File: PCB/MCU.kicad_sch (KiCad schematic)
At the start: 42 parts, among them J1 SWD, J10 GPIO2, J2 TC2030-NL, J3 VIK Keyboard Expansion, J4 OLED Breakout, J7 GND, J8 3V3, J9 GPIO3, SW1 PTS645, SW2 PTS645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

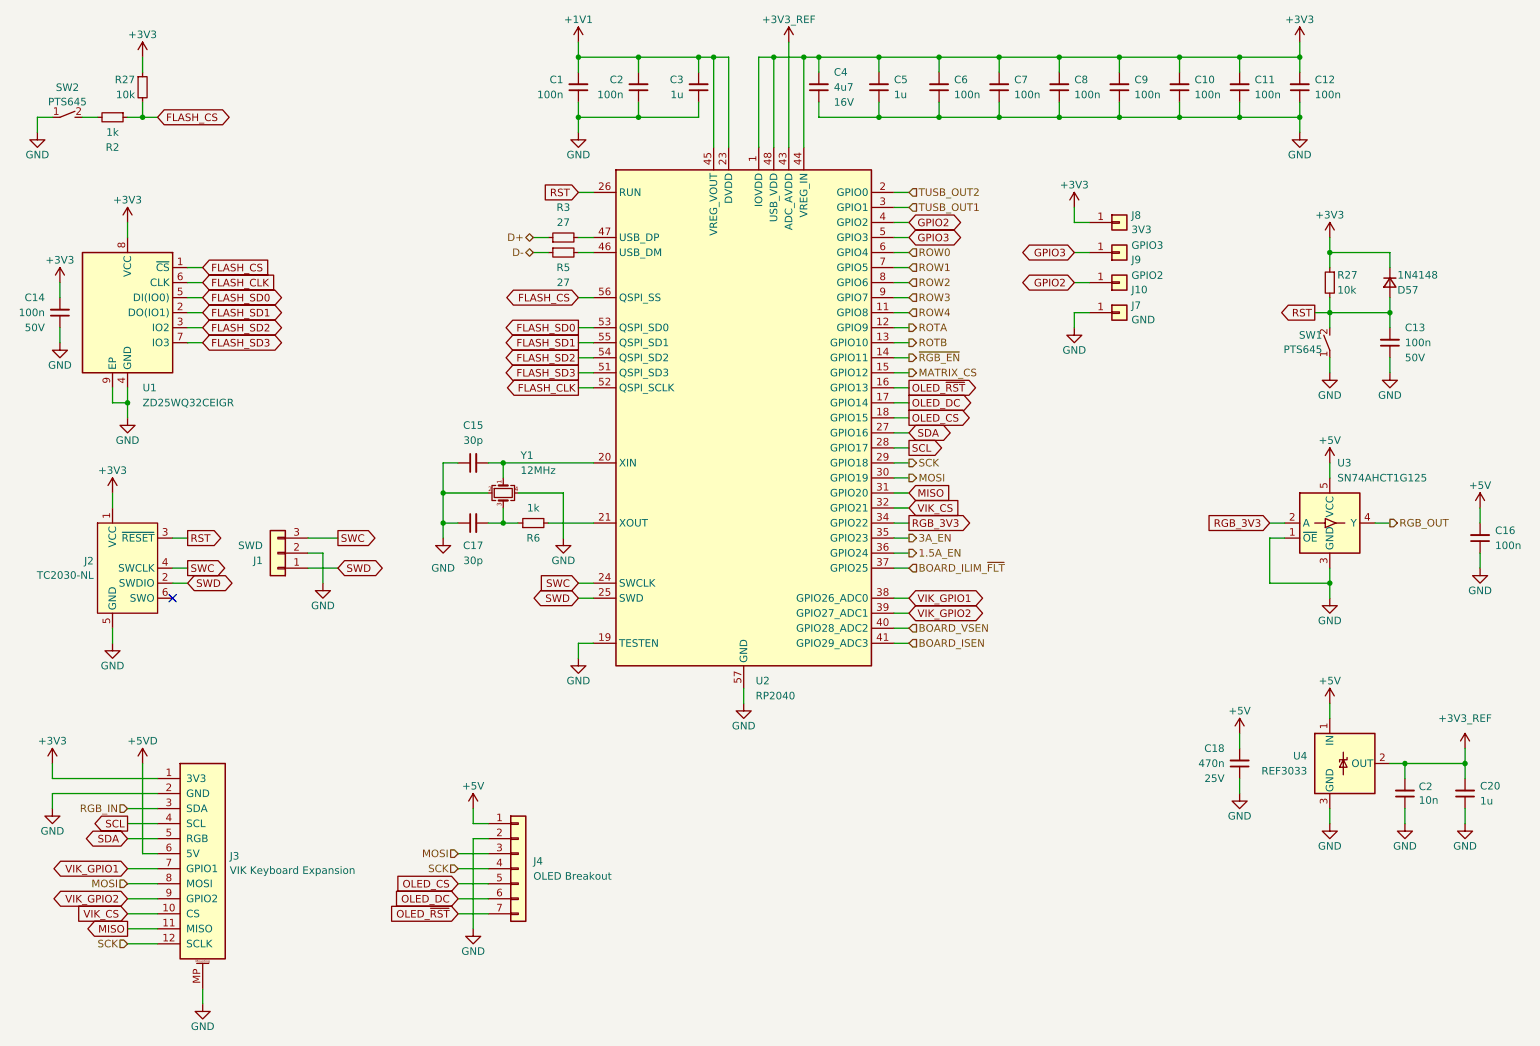
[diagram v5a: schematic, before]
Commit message: 16/08/2023 update
Updated to V3.1. Fixed VIK wiring (RGB and SDA were swapped). Added another BAV70 for the bottom button in the thumb cluster. Added DNP attribute to R15. Added jumper for VIK 5V rail.
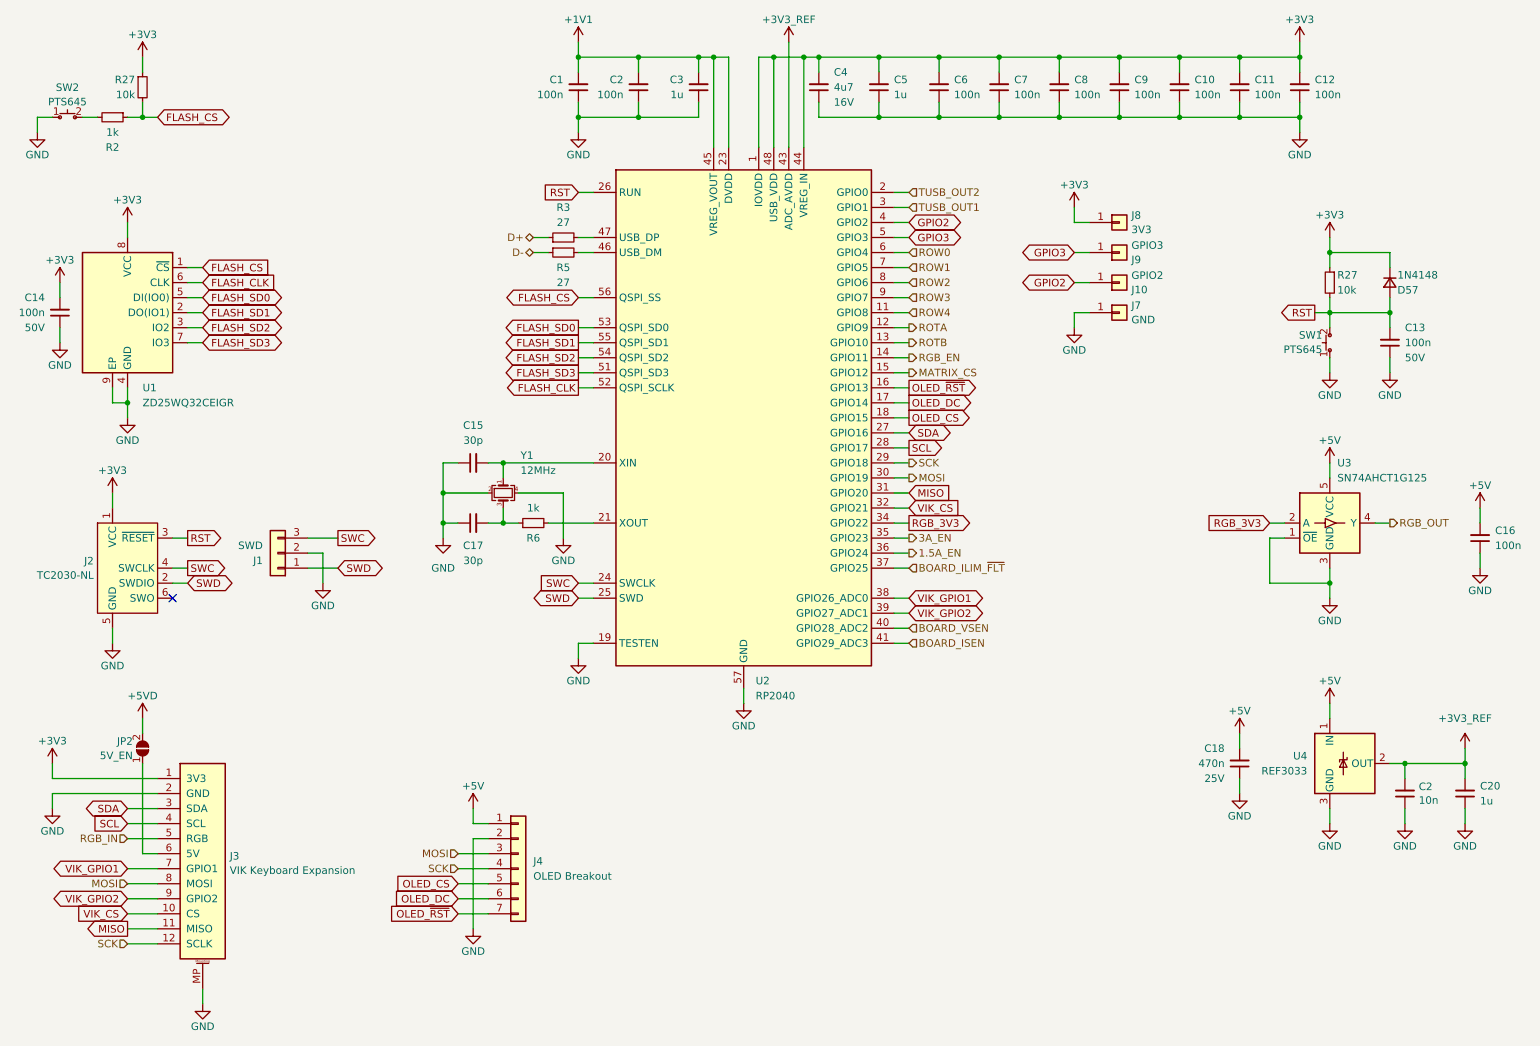
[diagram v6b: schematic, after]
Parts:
- added JP2: 5V_EN, Jumper:SolderJumper-2_P1.3mm_Open_Pad1.0x1.5mm, symbol Honeydew:SolderJumper_2_Open
- SW1, SW2: symbol Cantaloupe:SW_SPST_Small -> Honeydew:SW_SPST_Small
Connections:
- net +5VD: now also JP2.2 (B); no longer J3.6 (5V)
- net RGB_IN: now also J3.5 (RGB); no longer J3.3 (SDA)
- net SDA: now also J3.3 (SDA); no longer J3.5 (RGB)
- net ~{RGB_EN} renamed RGB_EN
- new net: J3.6 (5V), JP2.1 (A)
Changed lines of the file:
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@@
   (title_block
     (title "Honeydew unified split ergonomic keyboard")
-    (date "2023-08-06")
-    (rev "V3.0")
+    (date "2023-08-16")
+    (rev "V3.1")
     (company "Created by Ariamelon (https://github.com/Ariamelon/Honeydew/)")
     (comment 1 "All capacitors 50V unless otherwise specified.")
-    (comment 2 "Licensed under CC BY 4.0.")
+    (comment 2 "Follows the VIK standard by Sadek Baroudi (https://github.com/sadekbaroudi/VIK)")
+    (comment 3 "Licensed under CC BY 4.0.")
   )
   (junction (at 180.34 35.56) (diameter 0) (color 0 0 0 0)
@@
     (stroke (width 0) (type default))
   )
+  (wire (pts (xy 35.56 144.78) (xy 35.56 160.02))
+    (stroke (width 0) (type default))
+  )
   (wire (pts (xy 149.86 25.4) (xy 160.02 25.4))
     (stroke (width 0) (type default))
@@
     (stroke (width 0) (type default))
   )
-  (wire (pts (xy 35.56 144.78) (xy 35.56 160.02))
+  (wire (pts (xy 35.56 137.16) (xy 35.56 139.7))
     (stroke (width 0) (type default))
   )
@@
     )
   )
-  (global_label "SDA" (shape bidirectional) (at 33.02 157.48 180) (fields_autoplaced)
+  (global_label "SDA" (shape bidirectional) (at 33.02 152.4 180) (fields_autoplaced)
     (effects (font (size 1.27 1.27)) (justify right))
-    (property "Intersheetrefs" "${INTERSHEET_REFS}" (at 26.1684 157.48 0)
+    (property "Intersheetrefs" "${INTERSHEET_REFS}" (at 26.1684 152.4 0)
       (effects (font (size 1.27 1.27)) (justify right) hide)
     )
@@
     )
   )
-  (global_label "SCL" (shape output) (at 33.02 154.94 180) (fields_autoplaced)
+  (global_label "SCL" (shape input) (at 33.02 154.94 180) (fields_autoplaced)
     (effects (font (size 1.27 1.27)) (justify right))
     (property "Intersheetrefs" "${INTERSHEET_REFS}" (at 27.1814 154.94 0)
@@
     (effects (font (size 1.27 1.27)) (justify right))
   )
-  (hierarchical_label "RGB_IN" (shape input) (at 33.02 152.4 180) (fields_autoplaced)
+  (hierarchical_label "RGB_IN" (shape input) (at 33.02 157.48 180) (fields_autoplaced)
     (effects (font (size 1.27 1.27)) (justify right))
   )
@@
     (effects (font (size 1.27 1.27)) (justify left))
   )
-  (hierarchical_label "~{RGB_EN}" (shape output) (at 165.1 76.2 0) (fields_autoplaced)
+  (hierarchical_label "RGB_EN" (shape output) (at 165.1 76.2 0) (fields_autoplaced)
     (effects (font (size 1.27 1.27)) (justify left))
   )
@@
     )
   )
-  (symbol (lib_id "Cantaloupe:SW_SPST_Small") (at 236.22 73.66 90) (unit 1)
+  (symbol (lib_id "Honeydew:SW_SPST_Small") (at 236.22 73.66 90) (unit 1)
     (in_bom yes) (on_board yes) (dnp no)
     (property "Reference" "SW1" (at 234.95 72.39 90)
@@
       (effects (font (size 1.524 1.524)) hide)
     )
-    (property "Datasheet" "" (at 231.14 73.66 0)
+    (property "Datasheet" "~" (at 231.14 73.66 0)
       (effects (font (size 1.524 1.524)) hide)
     )
@@
     )
   )
-  (symbol (lib_id "power:+5VD") (at 35.56 144.78 0) (unit 1)
+  (symbol (lib_id "power:+5VD") (at 35.56 137.16 0) (unit 1)
     (in_bom yes) (on_board yes) (dnp no) (fields_autoplaced)
-    (property "Reference" "#PWR0110" (at 35.56 148.59 0)
+    (property "Reference" "#PWR0110" (at 35.56 140.97 0)
       (effects (font (size 1.27 1.27)) hide)
     )
-    (property "Value" "+5VD" (at 35.56 140.97 0)
+    (property "Value" "+5VD" (at 35.56 133.35 0)
       (effects (font (size 1.27 1.27)))
     )
-    (property "Footprint" "" (at 35.56 144.78 0)
+    (property "Footprint" "" (at 35.56 137.16 0)
       (effects (font (size 1.27 1.27)) hide)
     )
-    (property "Datasheet" "" (at 35.56 144.78 0)
+    (property "Datasheet" "" (at 35.56 137.16 0)
       (effects (font (size 1.27 1.27)) hide)
     )
@@
     )
   )
+  (symbol (lib_id "Honeydew:SolderJumper_2_Open") (at 35.56 142.24 270) (mirror x) (unit 1)
+    (in_bom no) (on_board yes) (dnp no)
+    (property "Reference" "JP2" (at 33.909 141.0279 90)
+      (effects (font (size 1.27 1.27)) (justify right))
+    )
+    (property "Value" "5V_EN" (at 33.909 143.4521 90)
+      (effects (font (size 1.27 1.27)) (justify right))
+    )
+    (property "Footprint" "Jumper:SolderJumper-2_P1.3mm_Open_Pad1.0x1.5mm" (at 35.56 142.24 0)
+      (effects (font (size 1.27 1.27)) hide)
+    )
+    (property "Datasheet" "~" (at 35.56 142.24 0)
+      (effects (font (size 1.27 1.27)) hide)
+    )
+    (pin "1")
+    (pin "2")
+    (instances
+      (project "Honeydew"
+        (path "/534caec7-cf60-4f90-b1ed-42c9d445ef0f/d133c1c6-f35d-4b98-81a0-3607ab1d2de1"
+          (reference "JP2") (unit 1)
+        )
+      )
+    )
+  )
   (symbol (lib_id "power:GND") (at 236.22 78.74 0) (unit 1)
     (in_bom yes) (on_board yes) (dnp no)
@@
     )
   )
-  (symbol (lib_id "Cantaloupe:SW_SPST_Small") (at 22.86 35.56 0) (unit 1)
+  (symbol (lib_id "Honeydew:SW_SPST_Small") (at 22.86 35.56 0) (unit 1)
     (in_bom yes) (on_board yes) (dnp no) (fields_autoplaced)
     (property "Reference" "SW2" (at 22.86 30.5267 0)
@@
       (effects (font (size 1.524 1.524)) hide)
     )
-    (property "Datasheet" "" (at 22.86 30.48 0)
+    (property "Datasheet" "~" (at 22.86 30.48 0)
       (effects (font (size 1.524 1.524)) hide)
     )

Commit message: 27/08/2023 update
Added unified library for all symbols, footprints and 3D files. Changed MCU to STM32F072RBT6. Removed OLED, voltage and current sensing, USB CC circuitry and shift registers. Changed ESD protection chip. Cleaned up routing and component placement. Changed SWD header pinout to 6-pin standard.
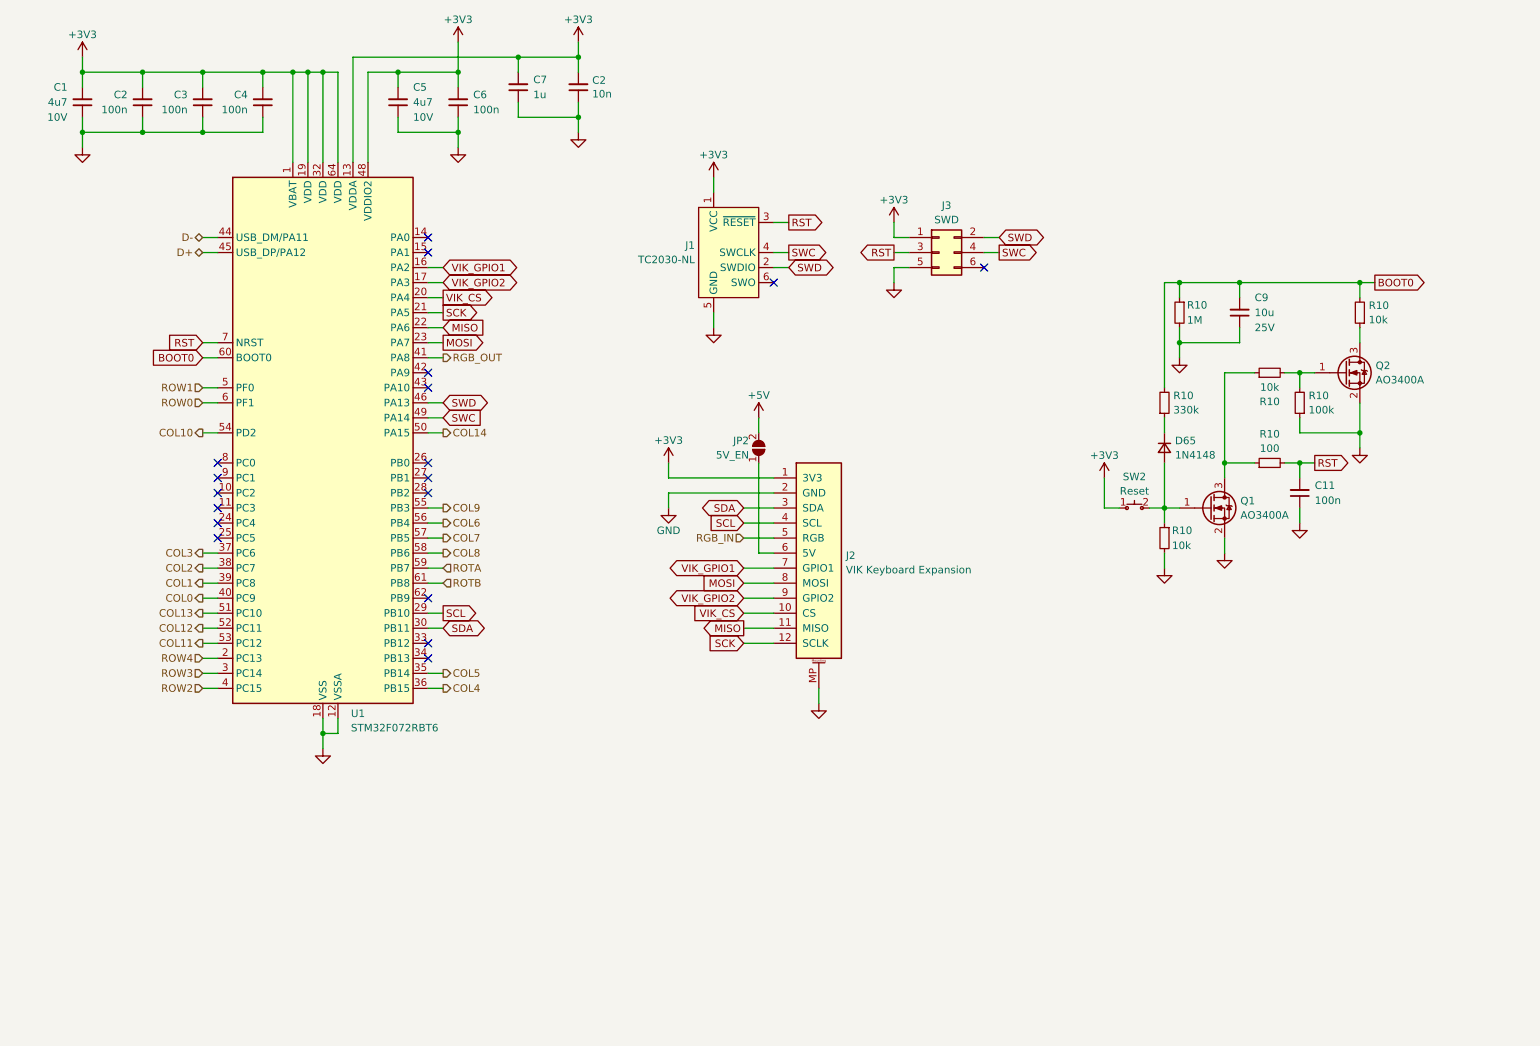
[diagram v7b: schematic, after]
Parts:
- removed C13, C14, C16, C2, C7, C8: 100n, Capacitor_SMD:C_0402_1005Metric, symbol Device:C_Small
- removed C15, C17: 30p, Capacitor_SMD:C_0402_1005Metric, symbol Device:C_Small
- removed C18: 470n, Capacitor_SMD:C_0603_1608Metric, symbol Device:C_Small
- removed C3, C5: 1u, Capacitor_SMD:C_0402_1005Metric, symbol Device:C_Small
- removed D57: 1N4148, Honeydew:D_SOD-323, symbol Device:D_Small
- removed J1: SWD, Honeydew:Header_SWD, symbol Connector_Generic:Conn_01x03
- removed J10: GPIO2, TestPoint:TestPoint_Pad_D1.5mm, symbol Connector_Generic:Conn_01x01
- removed J4: OLED Breakout, Honeydew:OLED_1.5_SSD1351_128x128, symbol Connector_Generic:Conn_01x07
- removed J7: GND, TestPoint:TestPoint_Pad_D1.5mm, symbol Connector_Generic:Conn_01x01
- removed J8: 3V3, TestPoint:TestPoint_Pad_D1.5mm, symbol Connector_Generic:Conn_01x01
- removed J9: GPIO3, TestPoint:TestPoint_Pad_D1.5mm, symbol Connector_Generic:Conn_01x01
- removed R2, R6: 1k, Resistor_SMD:R_0402_1005Metric, symbol Device:R_Small
- removed R27 (x2): 10k, Resistor_SMD:R_0402_1005Metric, symbol Device:R_Small
- removed R3, R5: 27, Resistor_SMD:R_0402_1005Metric, symbol Device:R_Small
- removed SW1, SW2: PTS645, Honeydew:SW_SPST_PTS645, symbol Honeydew:SW_SPST_Small
- removed U1: ZD25WQ32CEIGR, Honeydew:USON-8-1EP_3x2mm_P0.5mm_EP1.6x0.2mm, symbol Memory_Flash:W25Q32JVZP
- removed U2: RP2040, Honeydew:QFN-56-1EP_7x7mm_P0.4mm_EP3.2x3.2mm_ThermalVias, symbol MCU_RaspberryPi:RP2040
- removed U3: SN74AHCT1G125, Package_TO_SOT_SMD:SOT-353_SC-70-5, symbol Honeydew:SN74AHCT1G125
- removed U4: REF3033, Honeydew:SOT-23-3, symbol Reference_Voltage:REF3033
- removed Y1: 12MHz, Crystal:Crystal_SMD_3225-4Pin_3.2x2.5mm, symbol Device:Crystal_GND24_Small
- added C11: 100n, Ariamelon-Device:C_0402_1005Metric, symbol Device:C_Small
- added D65: 1N4148, Ariamelon-Device:D_SOD-323, symbol Device:D_Small
- added J3: SWD, Ariamelon-Header:PinHeader_SWD_2x03_P2.54mm_Vertical, symbol Connector_Generic:Conn_02x03_Odd_Even
- added Q1, Q2: AO3400A, Ariamelon-Package:SOT-23-3, symbol Transistor_FET:AO3400A
- added R10 (x3): 10k, Ariamelon-Device:R_0402_1005Metric, symbol Device:R_Small
- added R10: 100, Ariamelon-Device:R_0402_1005Metric, symbol Device:R_Small
- added R10: 1M, Ariamelon-Device:R_0402_1005Metric, symbol Device:R_Small
- added R10: 330k, Ariamelon-Device:R_0402_1005Metric, symbol Device:R_Small
- added R10: 100k, Ariamelon-Device:R_0402_1005Metric, symbol Device:R_Small
- added SW2: Reset, Button_Switch_SMD:SW_SPST_TL3342, symbol Ariamelon-Switch:SW_Push_Small
- added U1: STM32F072RBT6, Ariamelon-Package:LQFP-64_10x10mm_P0.5mm, symbol Ariamelon-IC:STM32F072R_8-B_Tx
- C1: value 100n -> 4u7; footprint Capacitor_SMD:C_0402_1005Metric -> Ariamelon-Device:C_0402_1005Metric; LCSC C307331 -> C23733; Voltage 50V -> 10V
- C2, C6: footprint Capacitor_SMD:C_0402_1005Metric -> Ariamelon-Device:C_0402_1005Metric
- C2: renamed from C10; footprint Capacitor_SMD:C_0402_1005Metric -> Ariamelon-Device:C_0402_1005Metric
- C3: renamed from C11; footprint Capacitor_SMD:C_0402_1005Metric -> Ariamelon-Device:C_0402_1005Metric
- C4: renamed from C12; footprint Capacitor_SMD:C_0402_1005Metric -> Ariamelon-Device:C_0402_1005Metric
- C5: renamed from C4; footprint Capacitor_SMD:C_0603_1608Metric -> Ariamelon-Device:C_0402_1005Metric; LCSC C19666 -> C23733; Voltage 16V -> 10V
- C7: renamed from C20; footprint Capacitor_SMD:C_0402_1005Metric -> Ariamelon-Device:C_0402_1005Metric
- C9: value 100n -> 10u; footprint Capacitor_SMD:C_0402_1005Metric -> Ariamelon-Device:C_0603_1608Metric; LCSC C307331 -> C96446; Voltage 50V -> 25V
- J2: renamed from J3; footprint Honeydew:vik-keyboard-connector-horizontal -> Ariamelon-Connector:VIK_Keyboard_Horizontal; symbol Honeydew:vik-keyboard-connector -> Ariamelon-Connector:VIK Keyboard Connector
- JP2: symbol Honeydew:SolderJumper_2_Open -> Ariamelon-Misc:SolderJumper_2_Open
- renumbered J2 to J1
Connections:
- net +1V1 is gone; now on net +3V3: C1.2
- net +3V3_REF is gone; now on net +3V3: C2.2, C7.2
- net +5VD is gone; now on net +5V: JP2.2 (B)
- net +3V3: now also J3.1 (Pin_1), SW2.1 (A), U1.1 (VBAT), U1.13 (VDDA), U1.19 (VDD), U1.32 (VDD), U1.48 (VDDIO2), U1.64 (VDD); no longer C9.2
- net D+: now also U1.45 (USB_DP/PA12)
- net D-: now also U1.44 (USB_DM/PA11)
- net GND: now also C11.1, J3.5 (Pin_5), Q1.2 (S), Q2.2 (S), R10.1, R10.2, R10.2, U1.12 (VSSA), U1.18 (VSS), U1.31 (VSS), U1.47 (VSS), U1.63 (VSS)
- net MISO: now also U1.22 (PA6)
- net MOSI: now also U1.23 (PA7)
- net RGB_OUT: now also U1.41 (PA8)
- net ROTA: now also U1.59 (PB7)
- net ROTB: now also U1.61 (PB8)
- net ROW0: now also U1.6 (PF1)
- net ROW1: now also U1.5 (PF0)
- net ROW2: now also U1.4 (PC15)
- net ROW3: now also U1.3 (PC14)
- net ROW4: now also U1.2 (PC13)
- net RST: now also C11.2, J3.3 (Pin_3), R10.2, U1.7 (NRST)
- net SCK: now also U1.21 (PA5)
- net SCL: now also U1.29 (PB10)
- net SDA: now also U1.30 (PB11)
- net SWC: now also J3.4 (Pin_4), U1.49 (PA14)
- net SWD: now also J3.2 (Pin_2), U1.46 (PA13)
- net VIK_CS: now also U1.20 (PA4)
- net VIK_GPIO1: now also U1.16 (PA2)
- net VIK_GPIO2: now also U1.17 (PA3)
- new net: Q1.3 (D), R10.1, R10.1
- new net: Q2.1 (G), R10.2, R10.2
- new net: D65.2 (A), Q1.1 (G), R10.1, SW2.2 (B)
- new net: D65.1 (K), R10.1
- new net: Q2.3 (D), R10.1
- new net BOOT0: C9.2, R10.1, R10.2, R10.2, U1.60 (BOOT0)
- new net COL0: U1.40 (PC9)
- new net COL1: U1.39 (PC8)
- new net COL10: U1.54 (PD2)
- new net COL11: U1.53 (PC12)
- new net COL12: U1.52 (PC11)
- new net COL13: U1.51 (PC10)
- new net COL14: U1.50 (PA15)
- new net COL2: U1.38 (PC7)
- new net COL3: U1.37 (PC6)
- new net COL4: U1.36 (PB15)
- new net COL5: U1.35 (PB14)
- new net COL6: U1.56 (PB4)
- new net COL7: U1.57 (PB5)
- new net COL8: U1.58 (PB6)
- new net COL9: U1.55 (PB3)
- no-connect marks 1 -> 18
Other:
- moved on the sheet: C2, C3, C4, C5, C6, C7, J1, J2, JP2
